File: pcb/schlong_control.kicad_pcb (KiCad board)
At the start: 2 copper layers, 88.9 x 80 mm, 42 parts, among them P1 Power Connector (120V AC), P2 Input, P3 Output, U1 74HC595, U2 MOC3063M, U3 MOC3063M, U4 MOC3063M, U5 MOC3063M, U6 MOC3063M, U7 LM7805

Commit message: rework design
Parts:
- removed REF** (x4): 1pin, Connectors:1pin
- added P4: Output, idc:IDC_Header_Straight_2x05_Pitch2.54mm, F.Cu at (128.9, 83.8)
- added R16: 360, Resistors_THT:R_Axial_DIN0207_L6.3mm_D2.5mm_P7.62mm_Horizontal, F.Cu at (110.5, 48.3)
- added R17: 360, Resistors_THT:R_Axial_DIN0207_L6.3mm_D2.5mm_P7.62mm_Horizontal, F.Cu at (118.1, 48.3)
- added R18: 360, Resistors_THT:R_Axial_DIN0207_L6.3mm_D2.5mm_P7.62mm_Horizontal, F.Cu at (123.2, 48.3)
- P1: value Power Connector (120V AC) -> Power Input (120V AC); footprint Connectors_Terminal_Blocks:TerminalBlock_Pheonix_MKDS1.5-2pol -> TerminalBlocks_Phoenix:TerminalBlock_Phoenix_MKDS1.5-2pol
- P2: value Input -> Power Thru (120V AC); footprint Connectors:IDC_Header_Straight_10pins -> TerminalBlocks_Phoenix:TerminalBlock_Phoenix_MKDS1.5-2pol
- P3: value Output -> Input; footprint Connectors:IDC_Header_Straight_10pins -> idc:IDC_Header_Straight_2x05_Pitch2.54mm
- R1, R2, R3: value 510 -> 4k7
- R6, R7, R8: value 360 -> 510
- moved P2 80.7 mm to (132.7, 44.5), turned to 90 degrees
- moved P1 74.7 mm to (57.8, 40.0), turned to 270 degrees
- moved P3 52.4 mm to (61.6, 94.0), turned to 180 degrees
- moved R8 49.2 mm to (116.8, 71.8), turned to 0 degrees
- moved R7 44.8 mm to (104.1, 71.8), turned to 0 degrees
- moved R6 38.5 mm to (91.4, 71.8), turned to 0 degrees
- moved R4 31.8 mm to (66.0, 71.8)
- moved R5 31.8 mm to (78.7, 71.8)
- moved R3 27.1 mm to (111.8, 77.5), turned to 180 degrees
- moved R1 19.7 mm to (78.7, 77.5)
- moved R2 19.7 mm to (91.4, 77.5)
- moved R10 14.0 mm to (72.4, 48.3)
- moved R12 14.0 mm to (85.1, 48.3)
- moved R14 14.0 mm to (97.8, 48.3)
- moved R13 11.4 mm to (92.7, 48.3)
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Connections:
- P2 pad 1: +12V -> /AC_P
- P2 pad 2: +12V -> /AC_N
- P3 pad 3: /~QH -> /MOSI
- P3 pad 4: /~QH -> /MOSI
- R1 pad 1: Net-(R1-Pad1) -> /SCK
- R1 pad 2: Net-(R1-Pad2) -> GND
- R10 pad 1: Net-(D3-Pad2) -> /AC_N
- R10 pad 2: Net-(R10-Pad2) -> Net-(D1-Pad3)
- R11 pad 1: /AC_N -> Net-(D2-Pad2)
- R11 pad 2: Net-(D3-Pad3) -> Net-(R11-Pad2)
- R12 pad 1: Net-(D4-Pad2) -> /AC_N
- R12 pad 2: Net-(R12-Pad2) -> Net-(D2-Pad3)
- R13 pad 1: /AC_N -> Net-(D3-Pad2)
- R13 pad 2: Net-(D4-Pad3) -> Net-(R13-Pad2)
- R14 pad 1: Net-(D5-Pad2) -> /AC_N
- R14 pad 2: Net-(R14-Pad2) -> Net-(D3-Pad3)
- R15 pad 1: /AC_N -> Net-(D4-Pad2)
- R15 pad 2: Net-(D5-Pad3) -> Net-(R15-Pad2)
- R2 pad 1: Net-(R2-Pad1) -> /~LATCH
- R2 pad 2: Net-(R2-Pad2) -> GND
- R3 pad 1: Net-(R3-Pad1) -> /MOSI
- R3 pad 2: Net-(R3-Pad2) -> GND
- R6 pad 1: Net-(D1-Pad2) -> Net-(R6-Pad1)
- R7 pad 1: /AC_N -> Net-(R7-Pad1)
- R7 pad 2: Net-(D1-Pad3) -> Net-(R7-Pad2)
- R8 pad 1: Net-(D2-Pad2) -> Net-(R8-Pad1)
- R9 pad 1: /AC_N -> Net-(D1-Pad2)
- R9 pad 2: Net-(D2-Pad3) -> Net-(R9-Pad2)
- U1 pad 1: Net-(R2-Pad2) -> Net-(R5-Pad2)
- U1 pad 15: Net-(R1-Pad2) -> Net-(R4-Pad2)
- U1 pad 2: Net-(R3-Pad2) -> Net-(R6-Pad2)
- U1 pad 3: Net-(R4-Pad2) -> Net-(R7-Pad2)
- U1 pad 4: Net-(R5-Pad2) -> Net-(R8-Pad2)
- U2 pad 1: Net-(R1-Pad1) -> Net-(R4-Pad1)
- U2 pad 6: Net-(R6-Pad2) -> Net-(R9-Pad2)
- U3 pad 1: Net-(R2-Pad1) -> Net-(R5-Pad1)
- U3 pad 6: Net-(R8-Pad2) -> Net-(R11-Pad2)
- U4 pad 1: Net-(R3-Pad1) -> Net-(R6-Pad1)
- U4 pad 6: Net-(R10-Pad2) -> Net-(R13-Pad2)
- U5 pad 1: Net-(R4-Pad1) -> Net-(R7-Pad1)
- U5 pad 6: Net-(R12-Pad2) -> Net-(R15-Pad2)
- U6 pad 1: Net-(R5-Pad1) -> Net-(R8-Pad1)
- U6 pad 6: Net-(R14-Pad2) -> Net-(R17-Pad2)
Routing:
- net GND: track 170.8 -> 0.00 mm, vias 1 -> 0
- net (no net): track 168.9 -> 0.00 mm
- net /AC_P: track 130.7 -> 0.00 mm
- net /AC_N: track 106.3 -> 0.00 mm
- net +12V: track 80.8 -> 0.00 mm, vias 3 -> 0
- net VCC: track 71.8 -> 0.00 mm, vias 5 -> 0
- net /SCK: track 60.6 -> 0.00 mm, vias 3 -> 0
- net /~LATCH: track 57.5 -> 0.00 mm
- net Net-(R1-Pad2): track 44.5 -> 0.00 mm, vias 2 -> 0
- net /~QH: track 38.2 -> 0.00 mm
- net /MOSI: track 34.6 -> 0.00 mm, vias 1 -> 0
- net Net-(R5-Pad2): track 33.9 -> 0.00 mm, vias 1 -> 0
- net Net-(R2-Pad2): track 28.2 -> 0.00 mm, vias 1 -> 0
- net Net-(D1-Pad3): track 25.3 -> 0.00 mm
- net Net-(D3-Pad3): track 25.3 -> 0.00 mm
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- added copper zone on B.Cu, net GND
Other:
- outline, holes or cut-outs redrawn
- board text added: "coon@c-base.org 03/2018"
- board text removed: "coon@c-base.org 09/2017"

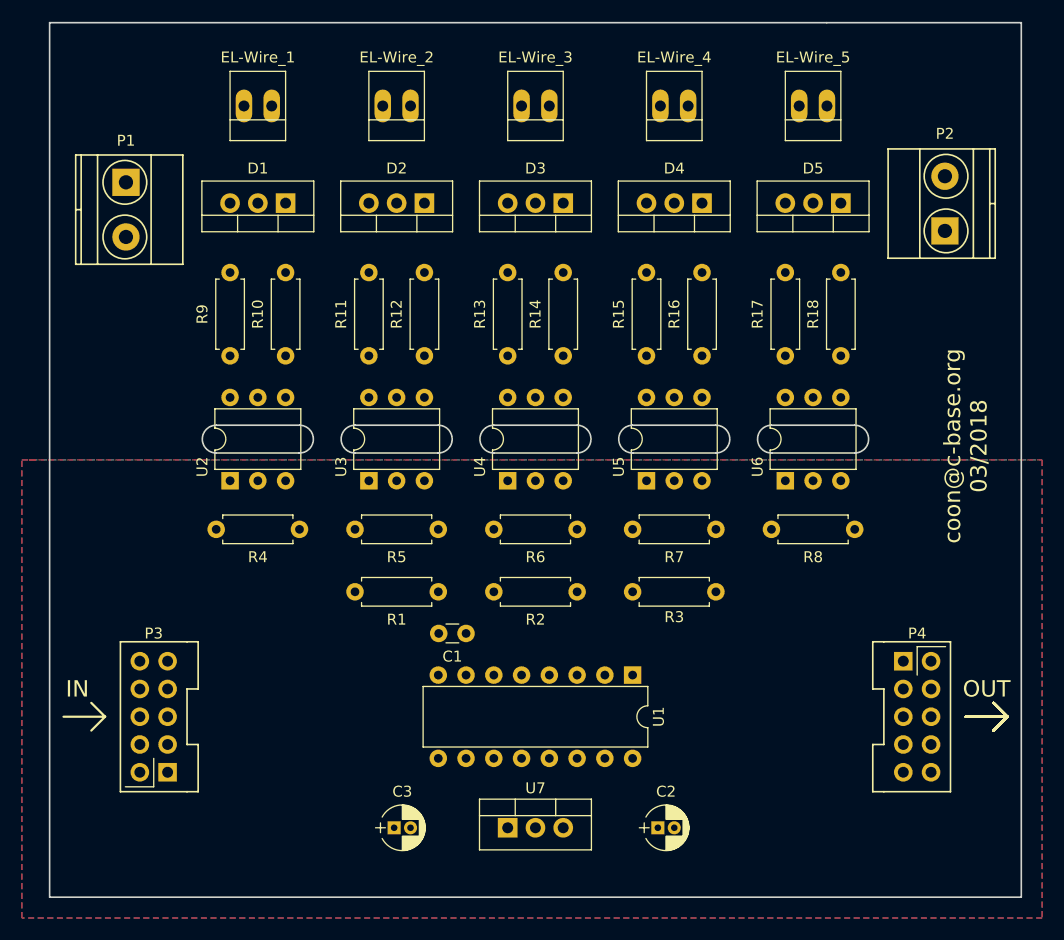
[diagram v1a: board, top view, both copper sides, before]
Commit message: pcb: add mounting holes + pin descriptions
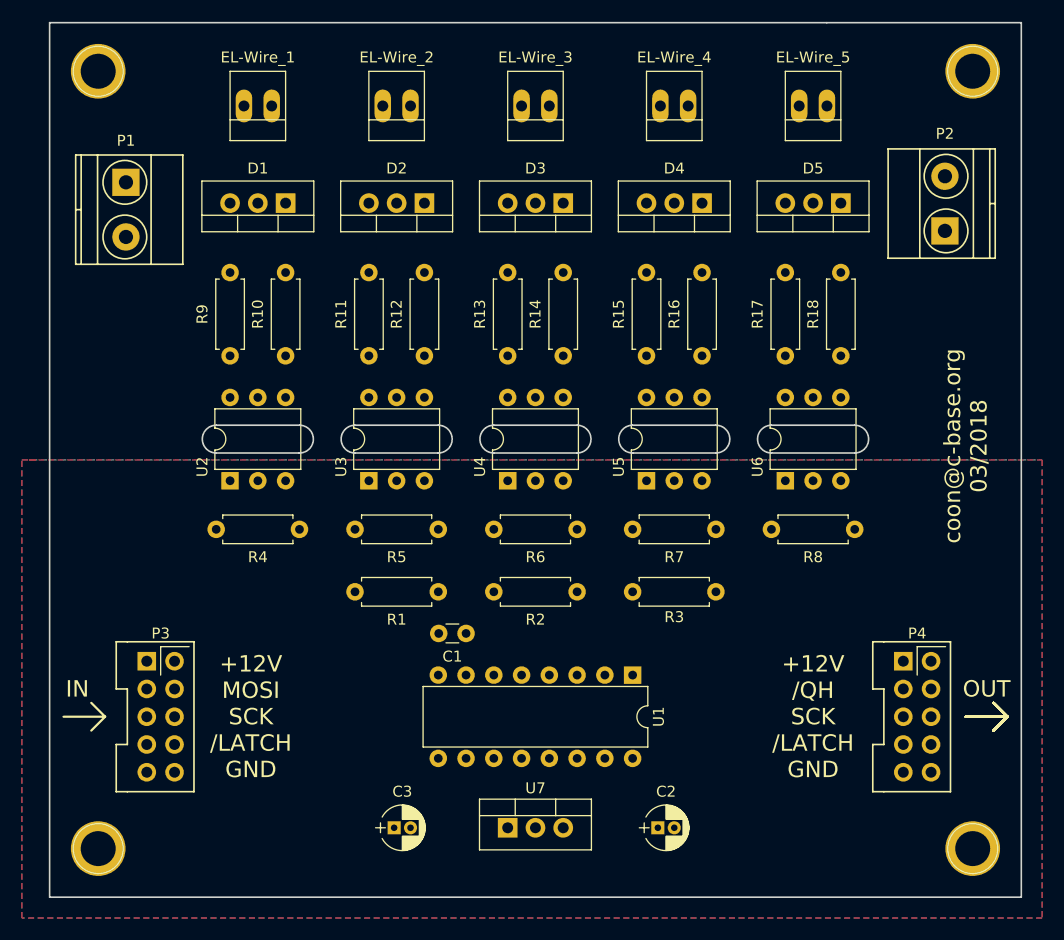
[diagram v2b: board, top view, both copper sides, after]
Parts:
- added REF**: 1pin, Connectors:1pin, F.Cu at (135.3, 101.0)
- added REF**: 1pin, Connectors:1pin, F.Cu at (55.2, 101.0)
- added REF**: 1pin, Connectors:1pin, F.Cu at (135.3, 29.8)
- added REF**: 1pin, Connectors:1pin, F.Cu at (55.2, 29.8)
- moved P3 10.3 mm to (59.7, 83.8), turned to 0 degrees
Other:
- board text added: "+12V /QH SCK /LATCH GND"
- board text added: "+12V MOSI SCK /LATCH GND"
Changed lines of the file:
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@@
     (area 50.724999 25.324999 139.775001 105.485001)
     (thickness 1.6)
-    (drawings 97)
+    (drawings 99)
     (tracks 0)
     (zones 0)
-    (modules 42)
+    (modules 46)
     (nets 35)
   )
@@
     (add_net "Net-(R9-Pad2)")
     (add_net VCC)
+  )
+  (module Connectors:1pin (layer F.Cu)
+    (at 135.255 100.965)
+    (descr "module 1 pin (ou trou mecanique de percage)")
+    (tags DEV)
+    (fp_text reference REF** (at 0 -3.048) (layer F.SilkS) hide
+      (effects (font (size 1 1) (thickness 0.15)))
+    )
+    (fp_text value 1pin (at 0 3) (layer F.Fab)
+      (effects (font (size 1 1) (thickness 0.15)))
+    )
+    (fp_circle (center 0 0) (end 2 0.8) (layer F.Fab) (width 0.1))
+    (fp_circle (center 0 0) (end 2.6 0) (layer F.CrtYd) (width 0.05))
+    (fp_circle (center 0 0) (end 0 -2.286) (layer F.SilkS) (width 0.12))
+    (pad 1 thru_hole circle (at 0 0) (size 5 5) (drill 3.2) (layers *.Cu *.Mask))
+  )
+  (module Connectors:1pin (layer F.Cu)
+    (at 55.245 100.965)
+    (descr "module 1 pin (ou trou mecanique de percage)")
+    (tags DEV)
+    (fp_text reference REF** (at 0 -3.048) (layer F.SilkS) hide
+      (effects (font (size 1 1) (thickness 0.15)))
+    )
+    (fp_text value 1pin (at 0 3) (layer F.Fab)
+      (effects (font (size 1 1) (thickness 0.15)))
+    )
+    (fp_circle (center 0 0) (end 2 0.8) (layer F.Fab) (width 0.1))
+    (fp_circle (center 0 0) (end 2.6 0) (layer F.CrtYd) (width 0.05))
+    (fp_circle (center 0 0) (end 0 -2.286) (layer F.SilkS) (width 0.12))
+    (pad 1 thru_hole circle (at 0 0) (size 5 5) (drill 3.2) (layers *.Cu *.Mask))
+  )
+  (module Connectors:1pin (layer F.Cu)
+    (at 135.255 29.845)
+    (descr "module 1 pin (ou trou mecanique de percage)")
+    (tags DEV)
+    (fp_text reference REF** (at 0 -3.048) (layer F.SilkS) hide
+      (effects (font (size 1 1) (thickness 0.15)))
+    )
+    (fp_text value 1pin (at 0 3) (layer F.Fab)
+      (effects (font (size 1 1) (thickness 0.15)))
+    )
+    (fp_circle (center 0 0) (end 2 0.8) (layer F.Fab) (width 0.1))
+    (fp_circle (center 0 0) (end 2.6 0) (layer F.CrtYd) (width 0.05))
+    (fp_circle (center 0 0) (end 0 -2.286) (layer F.SilkS) (width 0.12))
+    (pad 1 thru_hole circle (at 0 0) (size 5 5) (drill 3.2) (layers *.Cu *.Mask))
   )
   (module Connectors:PINHEAD1-2 (layer F.Cu)
@@
   )
   (module idc:IDC_Header_Straight_2x05_Pitch2.54mm (layer F.Cu)
-    (at 61.595 93.98 180)
+    (at 59.69 83.82)
     (descr "Through hole straight pin header, 2x05, 2.54mm pitch, double rows")
     (tags "Through hole pin header THT 2x05 2.54mm double row")
-    (fp_text reference P3 (at 1.27 12.7 180) (layer F.SilkS)
-      (effects (font (size 1 1) (thickness 0.15)))
-    )
-    (fp_text value Input (at 1.27 12.49 180) (layer F.Fab)
+    (fp_text reference P3 (at 1.27 -2.54) (layer F.SilkS)
+      (effects (font (size 1 1) (thickness 0.15)))
+    )
+    (fp_text value Input (at 1.27 12.49) (layer F.Fab)
       (effects (font (size 1 1) (thickness 0.15)))
     )
@@
     (fp_line (start 4.35 11.95) (end 4.35 -1.8) (layer F.CrtYd) (width 0.05))
     (fp_line (start 4.35 -1.8) (end -1.8 -1.8) (layer F.CrtYd) (width 0.05))
-    (fp_text user %R (at 1.27 5.08 270) (layer F.Fab)
-      (effects (font (size 1 1) (thickness 0.15)))
-    )
-    (pad 1 thru_hole rect (at 0 0 180) (size 1.7 1.7) (drill 1) (layers *.Cu *.Mask)
+    (fp_text user %R (at 1.27 5.08 90) (layer F.Fab)
+      (effects (font (size 1 1) (thickness 0.15)))
+    )
+    (pad 1 thru_hole rect (at 0 0) (size 1.7 1.7) (drill 1) (layers *.Cu *.Mask)
       (net 3 +12V))
-    (pad 2 thru_hole oval (at 2.54 0 180) (size 1.7 1.7) (drill 1) (layers *.Cu *.Mask)
+    (pad 2 thru_hole oval (at 2.54 0) (size 1.7 1.7) (drill 1) (layers *.Cu *.Mask)
       (net 3 +12V))
-    (pad 3 thru_hole oval (at 0 2.54 180) (size 1.7 1.7) (drill 1) (layers *.Cu *.Mask)
+    (pad 3 thru_hole oval (at 0 2.54) (size 1.7 1.7) (drill 1) (layers *.Cu *.Mask)
       (net 16 /MOSI))
-    (pad 4 thru_hole oval (at 2.54 2.54 180) (size 1.7 1.7) (drill 1) (layers *.Cu *.Mask)
+    (pad 4 thru_hole oval (at 2.54 2.54) (size 1.7 1.7) (drill 1) (layers *.Cu *.Mask)
       (net 16 /MOSI))
-    (pad 5 thru_hole oval (at 0 5.08 180) (size 1.7 1.7) (drill 1) (layers *.Cu *.Mask)
+    (pad 5 thru_hole oval (at 0 5.08) (size 1.7 1.7) (drill 1) (layers *.Cu *.Mask)
       (net 17 /SCK))
-    (pad 6 thru_hole oval (at 2.54 5.08 180) (size 1.7 1.7) (drill 1) (layers *.Cu *.Mask)
+    (pad 6 thru_hole oval (at 2.54 5.08) (size 1.7 1.7) (drill 1) (layers *.Cu *.Mask)
       (net 17 /SCK))
-    (pad 7 thru_hole oval (at 0 7.62 180) (size 1.7 1.7) (drill 1) (layers *.Cu *.Mask)
+    (pad 7 thru_hole oval (at 0 7.62) (size 1.7 1.7) (drill 1) (layers *.Cu *.Mask)
       (net 18 /~LATCH))
-    (pad 8 thru_hole oval (at 2.54 7.62 180) (size 1.7 1.7) (drill 1) (layers *.Cu *.Mask)
+    (pad 8 thru_hole oval (at 2.54 7.62) (size 1.7 1.7) (drill 1) (layers *.Cu *.Mask)
       (net 18 /~LATCH))
-    (pad 9 thru_hole oval (at 0 10.16 180) (size 1.7 1.7) (drill 1) (layers *.Cu *.Mask)
+    (pad 9 thru_hole oval (at 0 10.16) (size 1.7 1.7) (drill 1) (layers *.Cu *.Mask)
       (net 2 GND))
-    (pad 10 thru_hole oval (at 2.54 10.16 180) (size 1.7 1.7) (drill 1) (layers *.Cu *.Mask)
+    (pad 10 thru_hole oval (at 2.54 10.16) (size 1.7 1.7) (drill 1) (layers *.Cu *.Mask)
       (net 2 GND))
     (model ${KISYS3DMOD}/Pin_Headers.3dshapes/Pin_Header_Straight_2x05_Pitch2.54mm.wrl
@@
     )
   )
+  (module Connectors:1pin (layer F.Cu)
+    (at 55.245 29.845)
+    (descr "module 1 pin (ou trou mecanique de percage)")
+    (tags DEV)
+    (fp_text reference REF** (at 0 -3.048) (layer F.SilkS) hide
+      (effects (font (size 1 1) (thickness 0.15)))
+    )
+    (fp_text value 1pin (at 0 3) (layer F.Fab)
+      (effects (font (size 1 1) (thickness 0.15)))
+    )
+    (fp_circle (center 0 0) (end 2 0.8) (layer F.Fab) (width 0.1))
+    (fp_circle (center 0 0) (end 2.6 0) (layer F.CrtYd) (width 0.05))
+    (fp_circle (center 0 0) (end 0 -2.286) (layer F.SilkS) (width 0.12))
+    (pad 1 thru_hole circle (at 0 0) (size 5 5) (drill 3.2) (layers *.Cu *.Mask))
+  )
+  (gr_text "+12V\n/QH\nSCK\n/LATCH\nGND" (at 120.65 88.9) (layer F.SilkS)
+    (effects (font (size 1.5 1.5) (thickness 0.3)))
+  )
+  (gr_text "+12V\nMOSI\nSCK\n/LATCH\nGND" (at 69.215 88.9) (layer F.SilkS)
+    (effects (font (size 1.5 1.5) (thickness 0.3)))
+  )
   (gr_line (start 55.88 88.9) (end 52.07 88.9) (angle 90) (layer F.SilkS) (width 0.2))
